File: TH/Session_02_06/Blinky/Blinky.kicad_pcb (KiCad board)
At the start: 2 copper layers, 38.1 x 38.1 mm, 13 parts, among them U1 TLC551CD‎

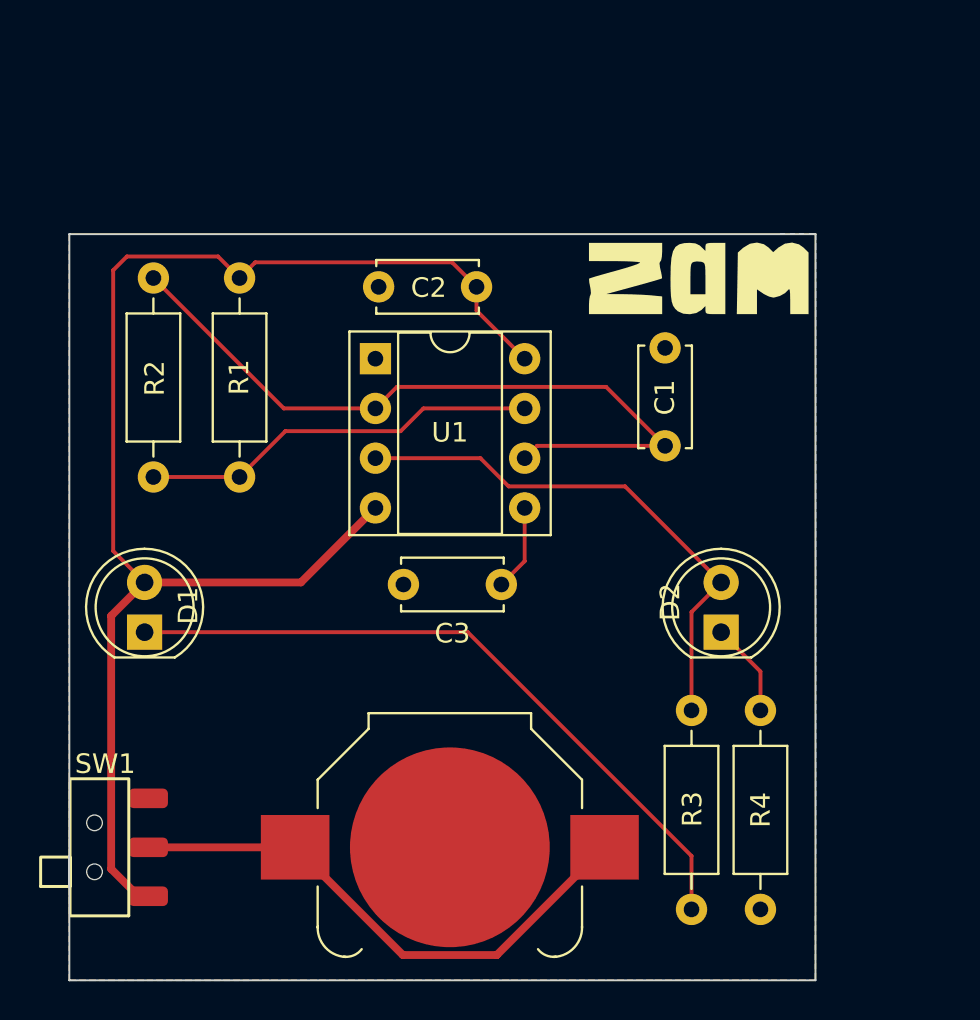
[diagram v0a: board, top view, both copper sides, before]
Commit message: Revamps the through-hole project as transistor based
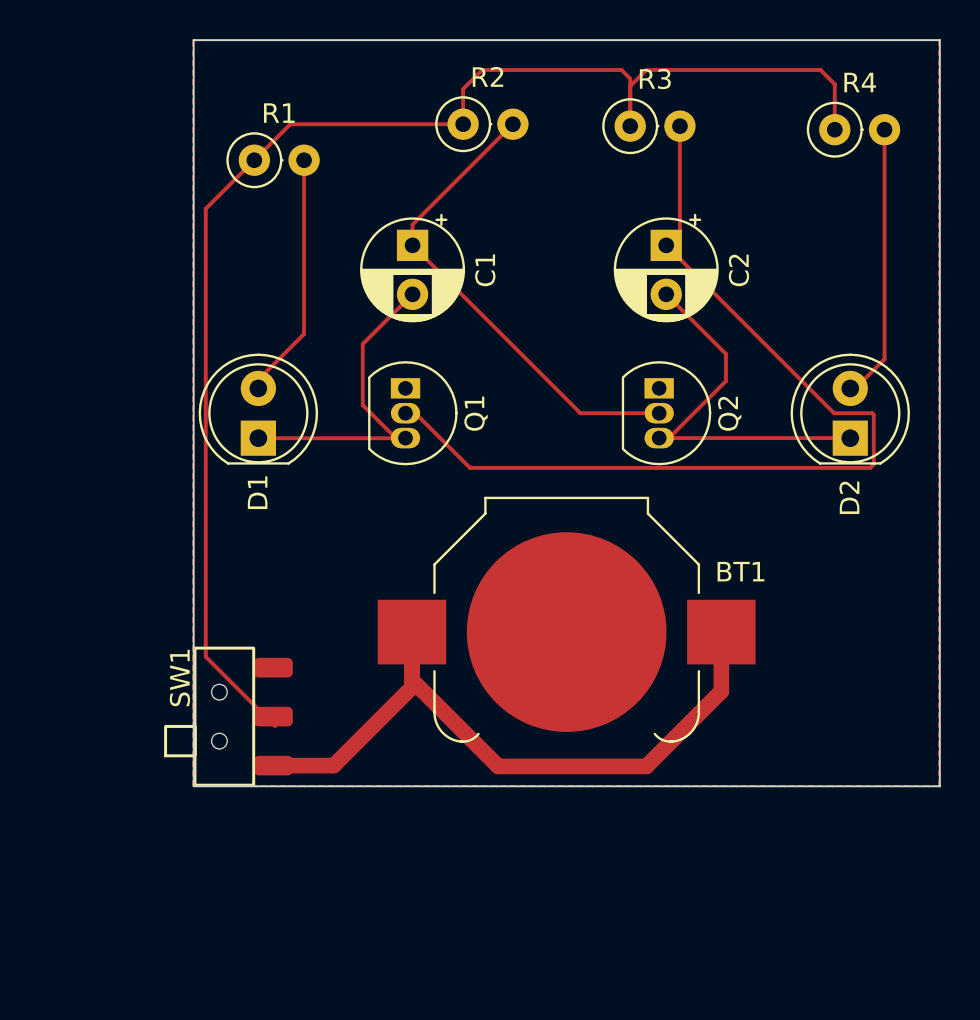
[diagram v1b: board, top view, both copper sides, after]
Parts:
- removed C3: 100nF, Capacitor_THT:C_Disc_D5.0mm_W2.5mm_P5.00mm
- removed SW?: SW_SPDT, Blinky_ZAM:SSK-1202
- removed U1: TLC551CD‎, Package_DIP:DIP-8_W7.62mm_Socket
- added Q1: 2N3904, Package_TO_SOT_THT:TO-92_Inline, F.Cu at (144.2, 84.1)
- added Q2: 2N3904, Package_TO_SOT_THT:TO-92_Inline, F.Cu at (157.1, 84.1)
- added SW1: SW_SPST, Blinky_ZAM:SSK-1202, F.Cu at (137.4, 100.8)
- C1: value 300nF -> 10μF; footprint Capacitor_THT:C_Disc_D5.0mm_W2.5mm_P5.00mm -> Capacitor_THT:CP_Radial_D5.0mm_P2.50mm
- C2: value 100nF -> 10μF; footprint Capacitor_THT:C_Disc_D5.0mm_W2.5mm_P5.00mm -> Capacitor_THT:CP_Radial_D5.0mm_P2.50mm
- LG2: footprint Blinky_ZAM:ZAM_LOGO_440 -> Blinky_ZAM:ZAM_LOGO_440_stopMask
- R1: value 10kΩ -> 220Ω; footprint Resistor_THT:R_Axial_DIN0207_L6.3mm_D2.5mm_P10.16mm_Horizontal -> Resistor_THT:R_Axial_DIN0207_L6.3mm_D2.5mm_P2.54mm_Vertical
- R2: value 1MΩ -> 100kΩ; footprint Resistor_THT:R_Axial_DIN0207_L6.3mm_D2.5mm_P10.16mm_Horizontal -> Resistor_THT:R_Axial_DIN0207_L6.3mm_D2.5mm_P2.54mm_Vertical
- R3: value 200Ω -> 100kΩ; footprint Resistor_THT:R_Axial_DIN0207_L6.3mm_D2.5mm_P10.16mm_Horizontal -> Resistor_THT:R_Axial_DIN0207_L6.3mm_D2.5mm_P2.54mm_Vertical
- R4: value 200Ω -> 220Ω; footprint Resistor_THT:R_Axial_DIN0207_L6.3mm_D2.5mm_P10.16mm_Horizontal -> Resistor_THT:R_Axial_DIN0207_L6.3mm_D2.5mm_P2.54mm_Vertical
- moved R3 40.1 mm to (155.6, 70.7), turned to 0 degrees
- moved R4 29.9 mm to (166.1, 70.9), turned to 0 degrees
- moved R2 24.0 mm to (147.1, 70.6), turned to 0 degrees
- moved LG2 22.3 mm to (169.2, 98.3), turned to 90 degrees
- moved C1 16.5 mm to (144.5, 76.8), turned to -90 degrees
- moved BT1 12.5 mm to (152.4, 96.5)
- moved D2 11.9 mm to (166.9, 86.6)
- moved D1 11.5 mm to (136.7, 86.6)
- moved C2 9.92 mm to (157.5, 76.8), turned to -90 degrees
- moved R1 6.06 mm to (136.4, 72.4), turned to 0 degrees
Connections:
- C1 pad 2: GND -> Net-(C1-Pad2)
- C2 pad 2: GND -> Net-(C2-Pad2)
- D1 pad 1: Net-(D1-Pad1) -> Net-(C1-Pad2)
- D1 pad 2: Net-(C2-Pad1) -> Net-(D1-Pad2)
- D2 pad 1: Net-(D2-Pad1) -> Net-(C2-Pad2)
- R1 pad 1: Net-(C2-Pad1) -> Net-(R1-Pad1)
- R1 pad 2: Net-(R1-Pad2) -> Net-(D1-Pad2)
- R2 pad 1: Net-(R1-Pad2) -> Net-(R1-Pad1)
- R3 pad 1: Net-(D1-Pad1) -> Net-(R1-Pad1)
- R3 pad 2: Net-(D2-Pad2) -> Net-(C2-Pad1)
- R4 pad 1: Net-(D2-Pad1) -> Net-(R1-Pad1)
- R4 pad 2: GND -> Net-(D2-Pad2)
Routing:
- net Net-(R1-Pad1): track 0.00 -> 71.6 mm
- net Net-(D1-Pad1): track 35.4 -> 0.00 mm
- net Net-(C2-Pad1): track 72.6 -> 48.2 mm
- net Net-(R1-Pad2): track 20.4 -> 0.00 mm
- net Net-(C2-Pad2): track 0.00 -> 20.1 mm
- net Net-(C1-Pad2): track 0.00 -> 17.1 mm
- net Net-(C1-Pad1): track 38.0 -> 24.5 mm
- net Net-(D2-Pad2): track 27.4 -> 14.2 mm
- net Net-(D1-Pad2): track 0.00 -> 13.2 mm
- net Net-(BT1-Pad1): track 27.9 -> 36.3 mm
- net Net-(D2-Pad1): track 4.83 -> 0.00 mm
- net Net-(C3-Pad1): track 4.40 -> 0.00 mm
- removed copper zone on B.Cu, net GND
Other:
- board text added: "Blinky Rev1"

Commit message: Makes corrections to the design rules
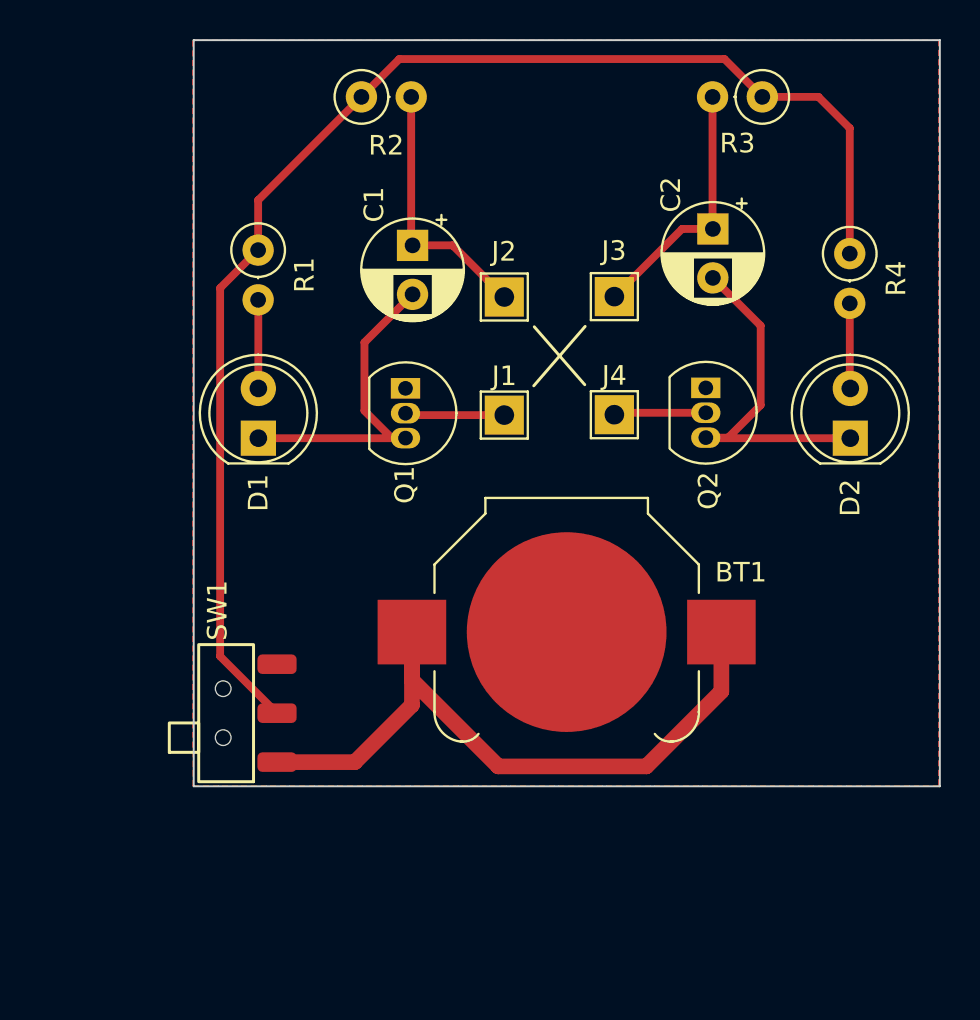
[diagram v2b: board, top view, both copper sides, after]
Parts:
- added J1: Jumper_1, TestPoint:TestPoint_THTPad_2.0x2.0mm_Drill1.0mm, F.Cu at (149.2, 85.4)
- added J2: Jumper_1, TestPoint:TestPoint_THTPad_2.0x2.0mm_Drill1.0mm, F.Cu at (149.2, 79.4)
- added J4: Jumper_1, TestPoint:TestPoint_THTPad_2.0x2.0mm_Drill1.0mm, F.Cu at (154.8, 85.4)
- added J?: Jumper_1, TestPoint:TestPoint_THTPad_2.0x2.0mm_Drill1.0mm, F.Cu at (154.8, 79.4)
- moved R3 6.91 mm to (162.4, 69.2), turned to 180 degrees
- moved R4 6.37 mm to (166.8, 77.2), turned to -90 degrees
- moved R2 5.38 mm to (141.9, 69.2)
- moved R1 4.59 mm to (136.6, 77.0), turned to -90 degrees
- moved C2 2.52 mm to (159.9, 75.9)
- moved Q2 2.38 mm to (159.5, 84.0)
- moved SW1 0.26 mm to (137.6, 100.7)
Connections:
- Q1 pad 2: Net-(C2-Pad1) -> Net-(J1-Pad1)
- Q2 pad 2: Net-(C1-Pad1) -> Net-(J4-Pad1)
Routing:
- net Net-(C2-Pad1): track 48.2 -> 13.2 mm
- net Net-(C1-Pad1): track 24.5 -> 13.4 mm
- net Net-(D2-Pad2): track 14.2 -> 4.36 mm
- net Net-(D1-Pad2): track 13.2 -> 4.53 mm
- net Net-(J1-Pad1): track 0.00 -> 5.08 mm
- net Net-(J4-Pad1): track 0.00 -> 4.71 mm
- net Net-(R1-Pad1): track 71.6 -> 69.3 mm
- net Net-(C2-Pad2): track 20.1 -> 18.4 mm
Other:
- board text added: "Blinky THT SS Rev1"
- board text removed: "Blinky Rev1"

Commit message: For the BOM
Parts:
- J1, J2, J4: value Jumper_1 -> bridge
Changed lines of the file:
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@@
       (outputformat 1)
       (mirror false)
-      (drillshape 1)
+      (drillshape 0)
       (scaleselection 1)
-      (outputdirectory "")
+      (outputdirectory "Gerbers/")
     )
   )
@@
       (effects (font (size 1 1) (thickness 0.15)))
     )
-    (fp_text value "Jumper_1" (at 0 2.05) (layer "F.Fab")
+    (fp_text value "bridge" (at 0 2.05) (layer "F.Fab")
       (effects (font (size 1 1) (thickness 0.15)))
     )
@@
       (effects (font (size 1 1) (thickness 0.15)))
     )
-    (fp_text value "Jumper_1" (at 0 2.05) (layer "F.Fab")
+    (fp_text value "bridge" (at 0 2.05) (layer "F.Fab")
       (effects (font (size 1 1) (thickness 0.15)))
     )
@@
       (effects (font (size 1 1) (thickness 0.15)))
     )
-    (fp_text value "Jumper_1" (at 0 2.05) (layer "F.Fab")
+    (fp_text value "bridge" (at 0 2.05) (layer "F.Fab")
       (effects (font (size 1 1) (thickness 0.15)))
     )
@@
       (effects (font (size 1 1) (thickness 0.15)))
     )
-    (fp_text value "Jumper_1" (at 0 2.05) (layer "F.Fab")
-      (effects (font (size 1 1) (thickness 0.15)))
-    )
+    (fp_text value "bridge" (at 0 2.05) (layer "F.Fab")
+      (effects (font (size 1 1) (thickness 0.15)))
+    )

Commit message: Corrections to the switch footprint
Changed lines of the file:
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@@
       (effects (font (size 1 1) (thickness 0.15)))
     )
-    (fp_rect (start -3.500001 -1.2) (end 3.500001 -4) (layer "F.SilkS") (width 0.1524) (fill none))
     (fp_rect (start -2 -5.499999) (end -0.5 -4) (layer "F.SilkS") (width 0.1524) (fill none))
+    (fp_rect (start -3.500001 -1.1) (end 3.500001 -4) (layer "F.SilkS") (width 0.1524) (fill none))
     (fp_rect (start -3.5 -5.5) (end 3.5 1) (layer "F.CrtYd") (width 0.01) (fill none))
-    (pad "" np_thru_hole circle (at -1.25 -2.75 90) (size 0.8 0.8) (drill 0.8) (layers F&B.Cu *.Mask))
-    (pad "" np_thru_hole circle (at 1.25 -2.75 90) (size 0.8 0.8) (drill 0.8) (layers F&B.Cu *.Mask))
+    (pad "" np_thru_hole circle (at -1.5 -2.75 90) (size 0.8 0.8) (drill 0.8) (layers F&B.Cu *.Mask))
+    (pad "" np_thru_hole circle (at 1.5 -2.75 90) (size 0.8 0.8) (drill 0.8) (layers F&B.Cu *.Mask))
     (pad "1" smd roundrect (at -2.5 0 90) (size 1 2) (layers "F.Cu" "F.Paste" "F.Mask") (roundrect_rratio 0.25)
       (net 1 "Net-(BT1-Pad1)") (pinfunction "A") (pintype "passive"))

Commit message: Correction to the NPN symbol to the purchased part Session_02_06 only
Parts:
- moved Q2 2.59 mm to (159.5, 86.6), turned to 90 degrees
- moved Q1 2.58 mm to (144.2, 86.7), turned to 90 degrees
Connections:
- Q1 pad 1: GND -> Net-(C1-Pad2)
- Q1 pad 3: Net-(C1-Pad2) -> GND
- Q2 pad 1: GND -> Net-(C2-Pad2)
- Q2 pad 3: Net-(C2-Pad2) -> GND
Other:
- board text added: "Blinky THT SS Rev1.1"
- board text removed: "Blinky THT SS Rev1"
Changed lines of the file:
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@@
   )
   (footprint "Package_TO_SOT_THT:TO-92_Inline" (layer "F.Cu")
-    (at 159.5 84.05 -90)
+    (at 159.5 86.64 90)
     (descr "TO-92 leads in-line, narrow, oval pads, drill 0.75mm (see NXP sot054_po.pdf)")
     (tags "to-92 sc-43 sc-43a sot54 PA33 transistor")
@@
     (fp_arc (start -0.483625 1.753625) (mid -1.021221 -0.949055) (end 1.27 -2.48) (layer "F.Fab") (width 0.1))
     (fp_arc (start 1.27 -2.48) (mid 3.561221 -0.949055) (end 3.023625 1.753625) (layer "F.Fab") (width 0.1))
-    (pad "1" thru_hole rect (at 0 0 270) (size 1.05 1.5) (drill 0.75) (layers *.Cu *.Mask)
+    (pad "1" thru_hole rect (at 0 0 90) (size 1.05 1.5) (drill 0.75) (layers *.Cu *.Mask)
+      (net 6 "Net-(C2-Pad2)") (pinfunction "C") (pintype "passive"))
+    (pad "2" thru_hole oval (at 1.27 0 90) (size 1.05 1.5) (drill 0.75) (layers *.Cu *.Mask)
+      (net 11 "Net-(J4-Pad1)") (pinfunction "B") (pintype "passive"))
+    (pad "3" thru_hole oval (at 2.54 0 90) (size 1.05 1.5) (drill 0.75) (layers *.Cu *.Mask)
       (net 2 "GND") (pinfunction "E") (pintype "passive"))
-    (pad "2" thru_hole oval (at 1.27 0 270) (size 1.05 1.5) (drill 0.75) (layers *.Cu *.Mask)
-      (net 11 "Net-(J4-Pad1)") (pinfunction "B") (pintype "passive"))
-    (pad "3" thru_hole oval (at 2.54 0 270) (size 1.05 1.5) (drill 0.75) (layers *.Cu *.Mask)
-      (net 6 "Net-(C2-Pad2)") (pinfunction "C") (pintype "passive"))
     (model "${KICAD6_3DMODEL_DIR}/Package_TO_SOT_THT.3dshapes/TO-92_Inline.wrl"
       (offset (xyz 0 0 0))
@@
   )
   (footprint "Package_TO_SOT_THT:TO-92_Inline" (layer "F.Cu")
-    (at 144.166 84.074 -90)
+    (at 144.16 86.65 90)
     (descr "TO-92 leads in-line, narrow, oval pads, drill 0.75mm (see NXP sot054_po.pdf)")
     (tags "to-92 sc-43 sc-43a sot54 PA33 transistor")
@@
     (fp_arc (start -0.483625 1.753625) (mid -1.021221 -0.949055) (end 1.27 -2.48) (layer "F.Fab") (width 0.1))
     (fp_arc (start 1.27 -2.48) (mid 3.561221 -0.949055) (end 3.023625 1.753625) (layer "F.Fab") (width 0.1))
-    (pad "1" thru_hole rect (at 0 0 270) (size 1.05 1.5) (drill 0.75) (layers *.Cu *.Mask)
+    (pad "1" thru_hole rect (at 0 0 90) (size 1.05 1.5) (drill 0.75) (layers *.Cu *.Mask)
+      (net 4 "Net-(C1-Pad2)") (pinfunction "C") (pintype "passive"))
+    (pad "2" thru_hole oval (at 1.27 0 90) (size 1.05 1.5) (drill 0.75) (layers *.Cu *.Mask)
+      (net 10 "Net-(J1-Pad1)") (pinfunction "B") (pintype "passive"))
+    (pad "3" thru_hole oval (at 2.54 0 90) (size 1.05 1.5) (drill 0.75) (layers *.Cu *.Mask)
       (net 2 "GND") (pinfunction "E") (pintype "passive"))
-    (pad "2" thru_hole oval (at 1.27 0 270) (size 1.05 1.5) (drill 0.75) (layers *.Cu *.Mask)
-      (net 10 "Net-(J1-Pad1)") (pinfunction "B") (pintype "passive"))
-    (pad "3" thru_hole oval (at 2.54 0 270) (size 1.05 1.5) (drill 0.75) (layers *.Cu *.Mask)
-      (net 4 "Net-(C1-Pad2)") (pinfunction "C") (pintype "passive"))
     (model "${KICAD6_3DMODEL_DIR}/Package_TO_SOT_THT.3dshapes/TO-92_Inline.wrl"
       (offset (xyz 0 0 0))
@@
   (gr_line (start 150.74 80.93) (end 153.32 83.89) (layer "F.SilkS") (width 0.15))
   (gr_rect (start 133.35 66.294) (end 171.45 104.394) (layer "Edge.Cuts") (width 0.1) (fill none))
-  (gr_text "Blinky THT\nSS Rev1" (at 165.22 103.8 90) (layer "F.Mask")
+  (gr_text "Blinky THT\nSS Rev1.1" (at 165.21999 103.799996 90) (layer "F.Mask")
     (effects (font (size 1 1) (thickness 0.15)) (justify left))
   )
